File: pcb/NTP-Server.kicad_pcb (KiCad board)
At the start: 2 copper layers, 85 x 68 mm, 21 parts, among them J1 Button1, J2 Button2, J3 USB_C, J4 Raspberry_Pi_2_3, J5 VCC-Monitor, J6 I2C, U1 GT-U7, U2 DS3231MZ

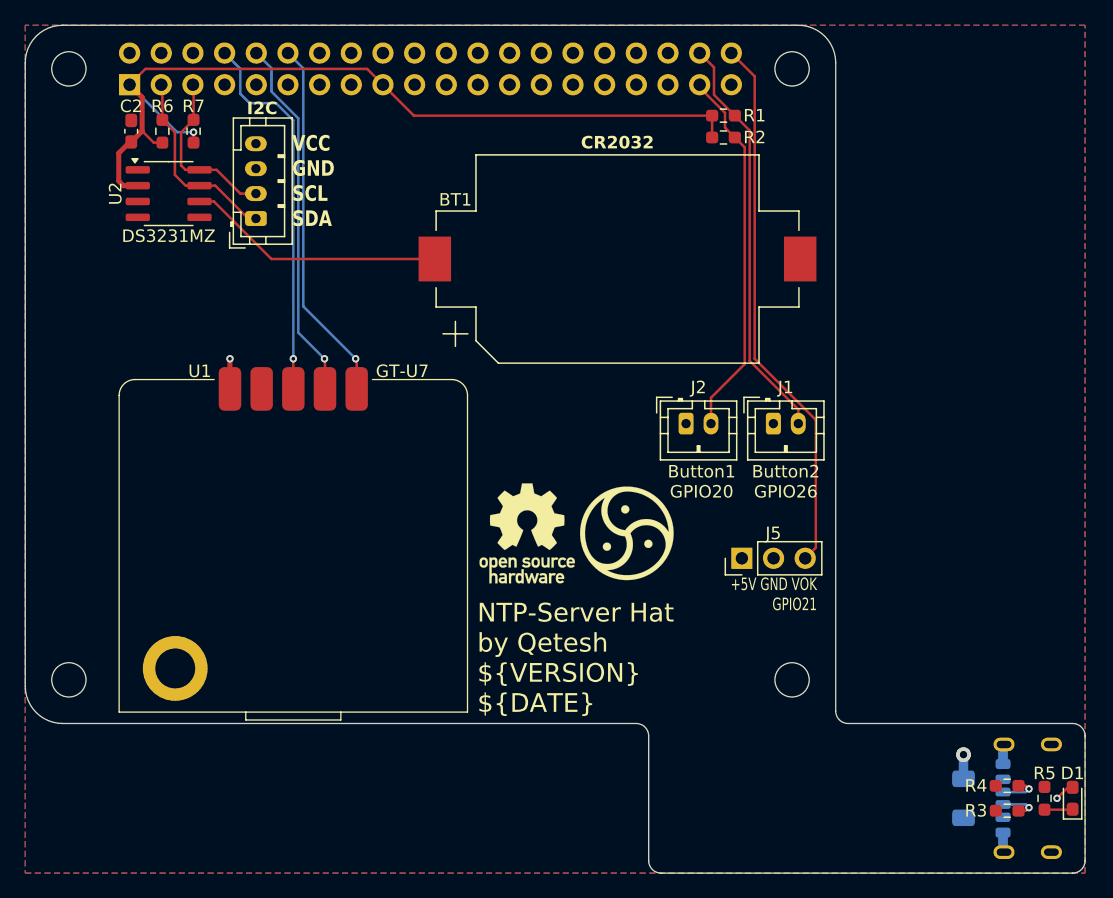
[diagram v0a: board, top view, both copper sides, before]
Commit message: feat!: complete redesign
Remove unneeded parts and make the whole board a lot smaller
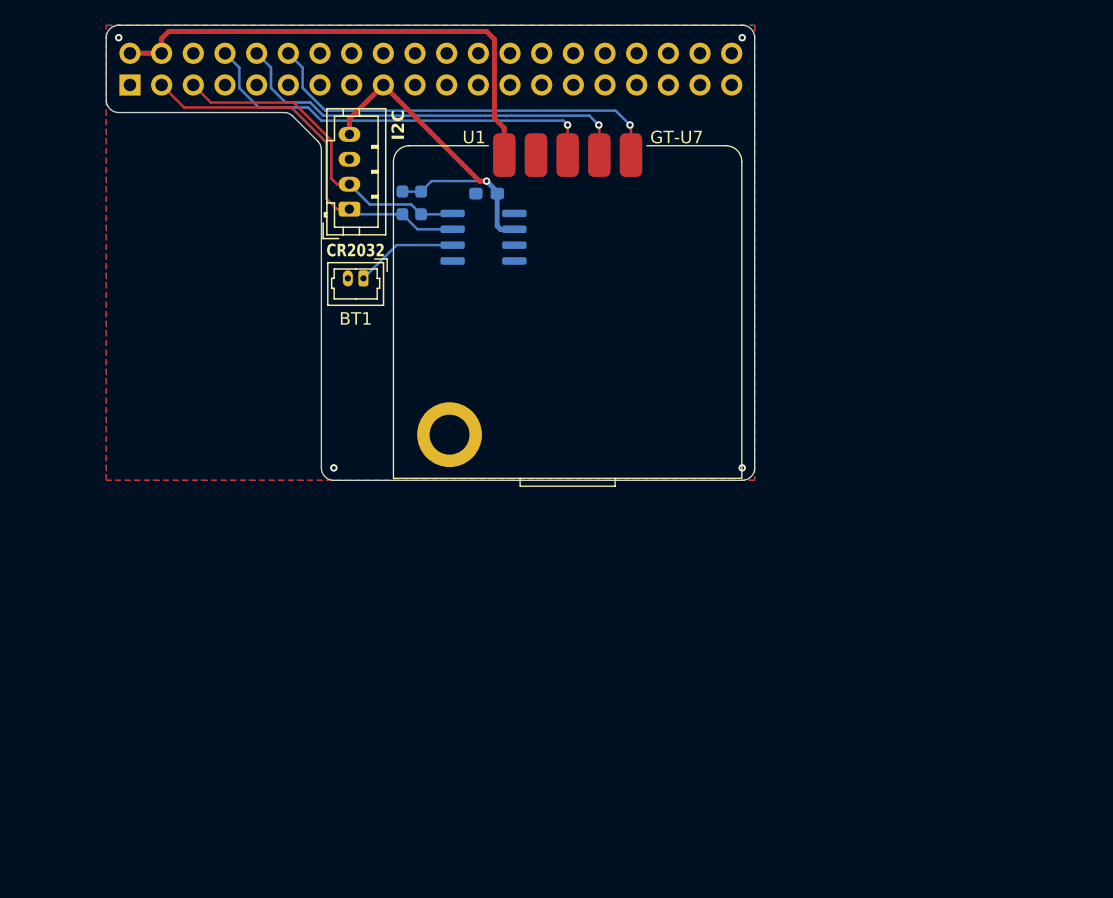
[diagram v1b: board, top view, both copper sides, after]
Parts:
- removed C1: 10u, Capacitor_SMD:C_1206_3216Metric_Pad1.33x1.80mm_HandSolder
- removed D1: Power, LED_SMD:LED_0603_1608Metric_Pad1.05x0.95mm_HandSolder
- removed J1: Button1, Connector_JST:JST_PH_B2B-PH-K_1x02_P2.00mm_Vertical
- removed J2: Button2, Connector_JST:JST_PH_B2B-PH-K_1x02_P2.00mm_Vertical
- removed J3: USB_C, Connector_USB:USB_C_Receptacle_GCT_USB4125-xx-x_6P_TopMnt_Horizontal
- removed J5: VCC-Monitor, Connector_PinHeader_2.54mm:PinHeader_1x03_P2.54mm_Vertical
- removed R1, R2: 10k, Resistor_SMD:R_0603_1608Metric_Pad0.98x0.95mm_HandSolder
- removed R3, R4: 5k1, Resistor_SMD:R_0603_1608Metric_Pad0.98x0.95mm_HandSolder
- removed R5: 1k2, Resistor_SMD:R_0603_1608Metric_Pad0.98x0.95mm_HandSolder
- BT1: footprint Battery:BatteryHolder_Keystone_1060_1x2032 -> Connector_Molex:Molex_PicoBlade_53047-0210_1x02_P1.25mm_Vertical
- C2, G***, REF**, U2: moved to B.Cu
- J4: footprint My_Footprints:RPi_HAT_FullSize -> Connector_PinSocket_2.54mm:PinSocket_2x20_P2.54mm_Vertical
- R6, R7: value 4k7 -> 2k2; moved to B.Cu
- moved C2 28.9 mm to (154.5, 60.0), turned to 180 degrees
- moved U1 28.9 mm to (161.0, 56.2)
- moved U2 25.5 mm to (154.2, 63.5), turned to 180 degrees
- moved G*** 24.6 mm to (171.0, 63.2), turned to 180 degrees
- moved REF** 24.4 mm to (163.2, 63.5), turned to 180 degrees
- moved J4 24.1 mm to (125.9, 51.3), turned to -90 degrees
- moved BT1 20.4 mm to (144.6, 66.8), turned to 180 degrees
- moved R6 20.1 mm to (147.8, 60.8), turned to -90 degrees
- moved R7 19.1 mm to (149.2, 60.8), turned to -90 degrees
- moved J6 7.54 mm to (143.5, 61.2)
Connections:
- J4 pad 1: +3V3 -> unconnected-(J4-3V3-Pad1)
- J4 pad 37: /Button2 -> unconnected-(J4-GPIO26-Pad37)
- J4 pad 38: /Button1 -> unconnected-(J4-GPIO20/MOSI1-Pad38)
- J4 pad 40: /VccOK -> unconnected-(J4-GPIO21/SCLK1-Pad40)
- J6 pad 4: +5V -> +3V3
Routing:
- net /VccOK: track 43.7 -> 0.00 mm
- net +3V3: track 70.8 -> 29.1 mm
- net +5V: track 3.28 -> 40.0 mm, vias 2 -> 0
- net /Button1: track 33.0 -> 0.00 mm
- net /Button2: track 29.8 -> 0.00 mm
- net /SDA: track 15.6 -> 30.8 mm
- net /SCL: track 13.8 -> 26.9 mm
- net /Batt+: track 20.8 -> 8.25 mm
- net GND: track 5.14 -> 0.00 mm, vias 1 -> 4
- net /GPS_RX: track 28.7 -> 32.7 mm
- net /GPS_PPS: track 28.7 -> 32.7 mm
- net /CC2: track 3.12 -> 0.00 mm, vias 1 -> 0
- net /CC1: track 3.12 -> 0.00 mm, vias 1 -> 0
- net /GPS_TX: track 30.0 -> 32.7 mm
- net Net-(D1-K): track 2.02 -> 0.00 mm
- added copper zone on B.Cu, net GND
- removed copper zone on B.Cu, net +5V
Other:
- board size 85 x 68 mm -> 52 x 36.5 mm
- board text added: "NTP-Server GPS Adapter by Qetesh ${VERSION} ${DATE}"
- board text removed: "+5V GND VOK GPIO21"
- board text removed: "Button1 GPIO20"
- board text removed: "Button2 GPIO26"
- board text removed: "NTP-Server Hat by Qetesh ${VERSION} ${DATE}"
- board text removed: "VCC GND SCL SDA"
